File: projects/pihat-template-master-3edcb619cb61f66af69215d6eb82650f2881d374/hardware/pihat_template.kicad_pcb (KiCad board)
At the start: 2 copper layers, 65 x 56.5 mm, 37 parts, among them P1 CONN_01X02, P2 CONN_01X02, P3 Raspberry_Pi_+_Conn, Q1 BSS138, U1 LM3489, U2 CAT24C32HU4I-GT3, U3 FDC5614P, U4 LM1117IMPX-ADJ, U5 DMMT5401

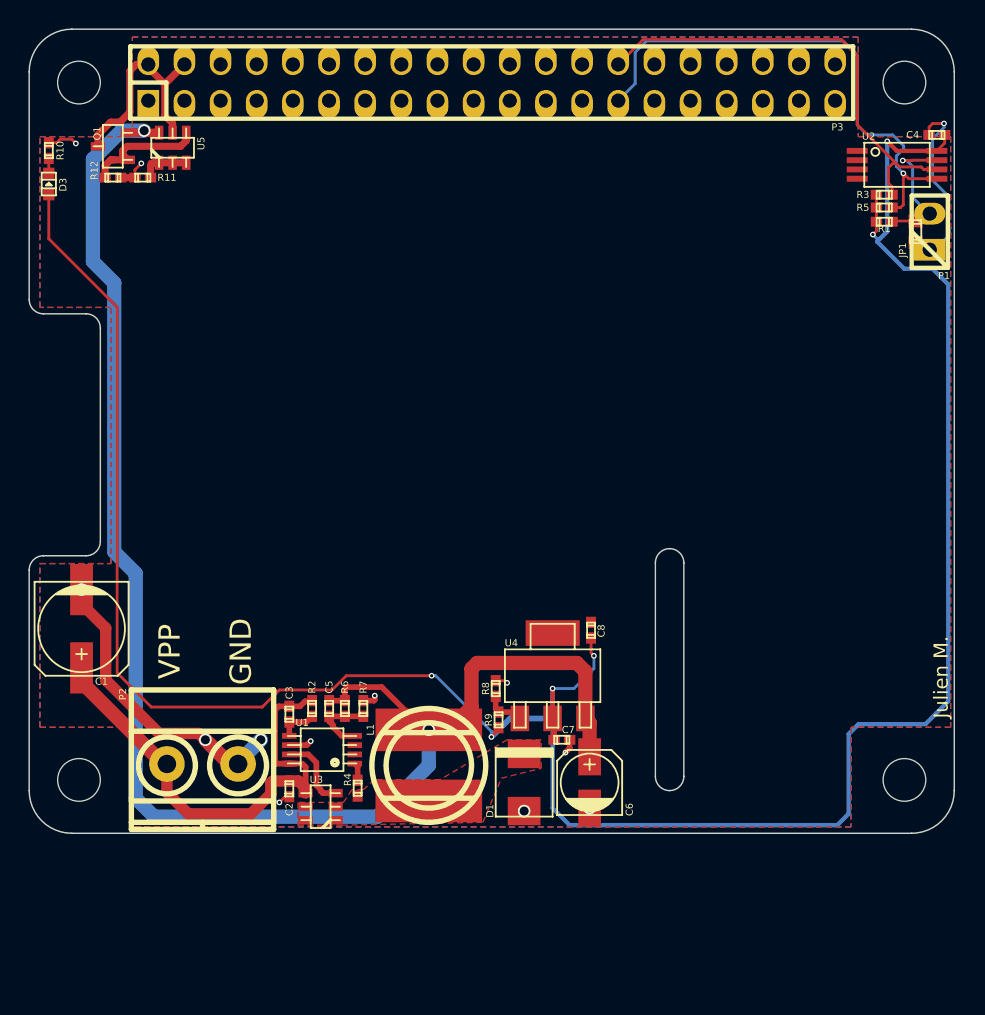
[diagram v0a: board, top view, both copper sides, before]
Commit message: Started placement of MAXM17503
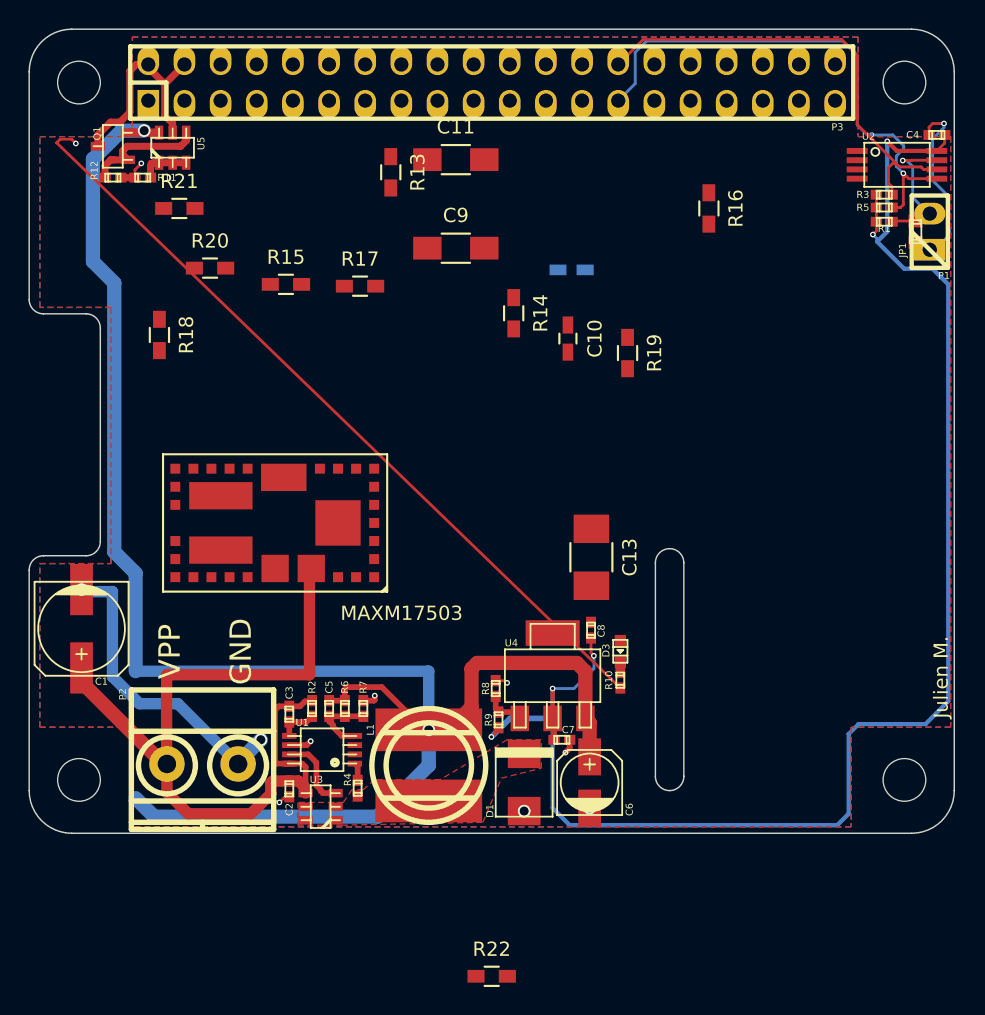
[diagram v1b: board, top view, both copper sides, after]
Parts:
- added C10: 11nF, Capacitors_SMD:C_0603_HandSoldering, F.Cu at (142.8, 92.8)
- added C11: 2.2uF, Capacitors_SMD:C_1206_HandSoldering, F.Cu at (134.9, 80.2)
- added C12: DNI, Capacitors_SMD:C_0603_HandSoldering, B.Cu at (143.0, 88.0)
- added C13: 22uF, Capacitors_SMD:C_1210_HandSoldering, F.Cu at (144.4, 108.2)
- added C9: 2.2uf, Capacitors_SMD:C_1206_HandSoldering, F.Cu at (134.9, 86.5)
- added R13: 3.3M, Resistors_SMD:R_0603_HandSoldering, F.Cu at (130.3, 81.1)
- added R14: 100K, Resistors_SMD:R_0603_HandSoldering, F.Cu at (139.0, 91.0)
- added R15: 100K, Resistors_SMD:R_0603_HandSoldering, F.Cu at (123.0, 89.0)
- added R16: 100K, Resistors_SMD:R_0603_HandSoldering, F.Cu at (152.7, 83.7)
- added R17: 26.7k, Resistors_SMD:R_0603_HandSoldering, F.Cu at (128.2, 89.1)
- added R18: 191k, Resistors_SMD:R_0603_HandSoldering, F.Cu at (114.1, 92.6)
- added R19: 42.2k, Resistors_SMD:R_0603_HandSoldering, F.Cu at (147.0, 93.8)
- added R20: 10k, Resistors_SMD:R_0603_HandSoldering, F.Cu at (117.6, 87.9)
- added R21: 10k, Resistors_SMD:R_0603_HandSoldering, F.Cu at (115.5, 83.7)
- added R22: .1, Resistors_SMD:R_0603_HandSoldering, F.Cu at (137.4, 137.6)
- added U6: MAXM17503, jvm:MAXM17503, F.Cu at (127.3, 102.0)
- moved R10 54.7 mm to (146.5, 116.8), turned to 90 degrees
- moved D3 51.9 mm to (146.5, 114.8), turned to 270 degrees
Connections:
- P3 pad 3: Net-(P3-Pad3) -> /jvm_options/SDA
- P3 pad 5: Net-(P3-Pad5) -> /jvm_options/SCL
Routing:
- net +3V3: track 176.1 -> 110.3 mm, vias 6 -> 5
- net GND: track 44.4 -> 99.7 mm, vias 13 -> 12
- net +24V: track 35.0 -> 58.2 mm
- net +5V: track 108.0 -> 123.8 mm

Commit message: update part placement 11-21-16
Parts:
- C12: moved to F.Cu
- moved C11 35.8 mm to (117.1, 111.3), turned to 270 degrees
- moved C13 32.1 mm to (115.8, 93.5), turned to 90 degrees
- moved R13 29.5 mm to (128.7, 110.6), turned to 0 degrees
- moved C9 29.0 mm to (120.9, 111.9), turned to 270 degrees
- moved R16 22.2 mm to (131.1, 88.8)
- moved C12 16.0 mm to (137.4, 103.0), turned to 180 degrees
- moved C10 15.8 mm to (133.3, 105.5), turned to 0 degrees
- moved R14 14.6 mm to (124.7, 87.7), turned to 180 degrees
- moved R17 11.5 mm to (133.8, 99.2), turned to 180 degrees
- moved R19 9.61 mm to (140.0, 100.4), turned to 180 degrees
- moved R18 6.17 mm to (119.7, 95.2)
- moved U6 3.89 mm to (125.4, 98.5)
- moved R15 3.10 mm to (124.7, 91.5), turned to 180 degrees
- moved R21 2.93 mm to (118.4, 83.9)
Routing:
- net GND: track 99.7 -> 43.0 mm, vias 12 -> 11
